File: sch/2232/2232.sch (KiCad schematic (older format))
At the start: 74 parts, among them J1 47346-0001, J2 IDC-06, J3 IDC-06, J4 IDC-10, J5 IDC-10, J6 6P6C, J7 Screw_Terminal_01x06, J8 Screw_Terminal_01x06, Q1 BC817-40, Q2 FZT1049A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

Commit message: Minor updates
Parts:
- R11, R12, R13, R8: value 100 -> 110
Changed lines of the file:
@@
 P 7600 2700
 F 0 "R8" V 7390 2700 50  0000 C CNN
-F 1 "100" V 7483 2700 50  0000 C CNN
+F 1 "110" V 7483 2700 50  0000 C CNN
 F 2 "NevaDA:R_0603" V 7530 2700 50  0001 C CNN
 F 3 "~" H 7600 2700 50  0001 C CNN
@@
 P 8000 2350
 F 0 "R13" H 8070 2397 50  0000 L CNN
-F 1 "100" H 8070 2304 50  0000 L CNN
+F 1 "110" H 8070 2304 50  0000 L CNN
 F 2 "NevaDA:R_0603" V 7930 2350 50  0001 C CNN
 F 3 "~" H 8000 2350 50  0001 C CNN
@@
 P 7150 2950
 F 0 "R11" H 7220 2997 50  0000 L CNN
-F 1 "100" H 7220 2904 50  0000 L CNN
+F 1 "110" H 7220 2904 50  0000 L CNN
 F 2 "NevaDA:R_0603" V 7080 2950 50  0001 C CNN
 F 3 "~" H 7150 2950 50  0001 C CNN
@@
 P 7150 3250
 F 0 "R12" H 7220 3297 50  0000 L CNN
-F 1 "100" H 7220 3204 50  0000 L CNN
+F 1 "110" H 7220 3204 50  0000 L CNN
 F 2 "NevaDA:R_0603" V 7080 3250 50  0001 C CNN
 F 3 "~" H 7150 3250 50  0001 C CNN

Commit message: Gerbers exported
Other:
- note added: "Sticky Pads virtual objects"
- moved on the sheet: C14, C15, C16, C17, C18, D1, D2, D3, D4, D5, D6, D7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

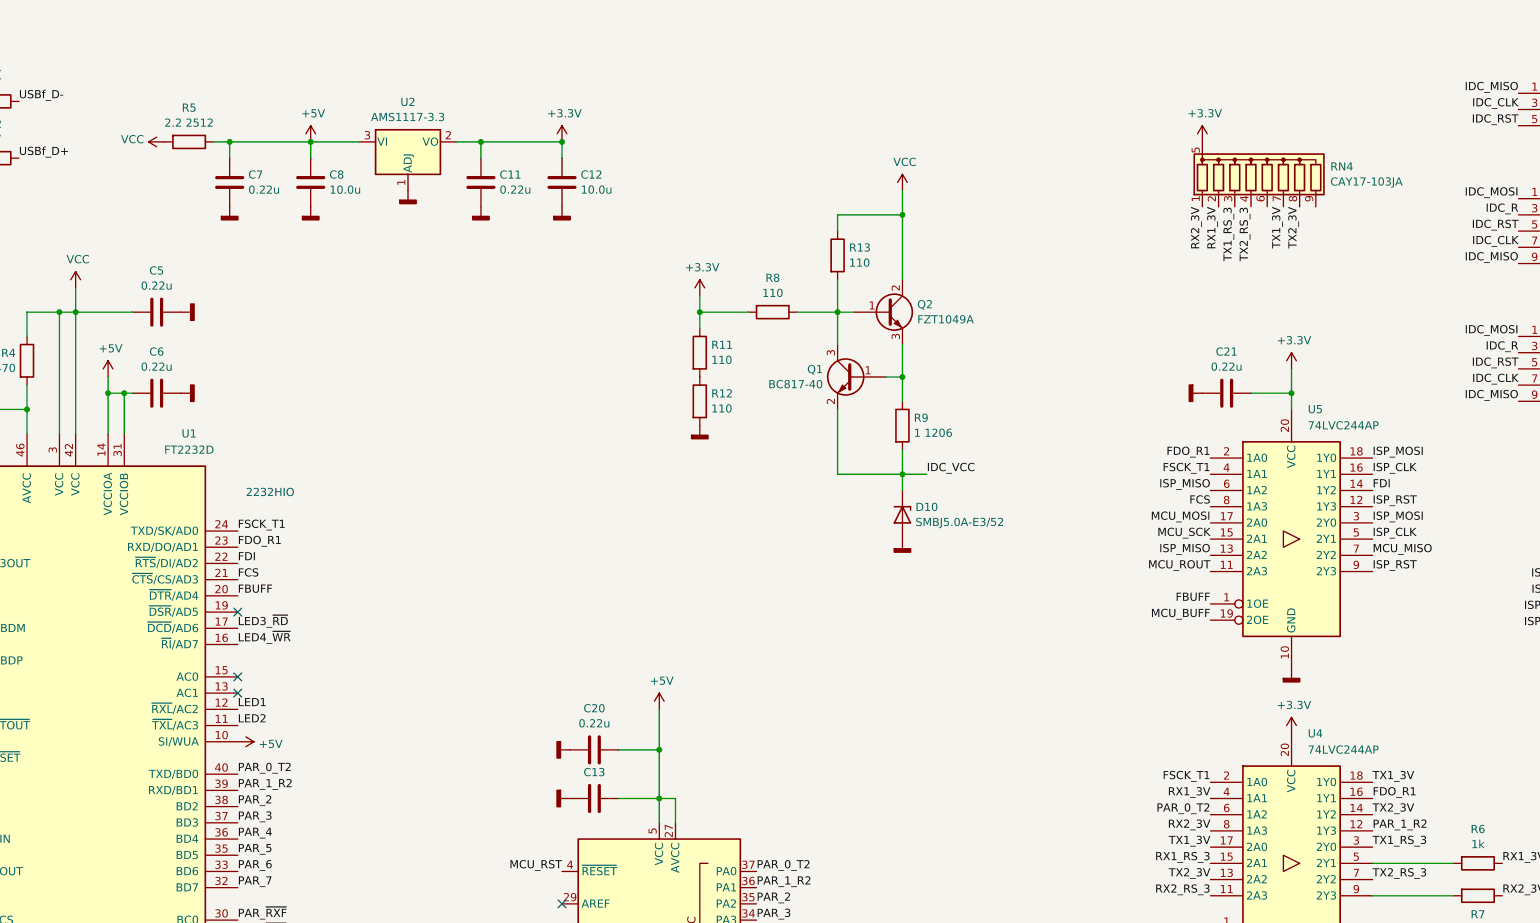
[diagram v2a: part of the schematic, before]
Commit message: Pullups to RST and MISO added
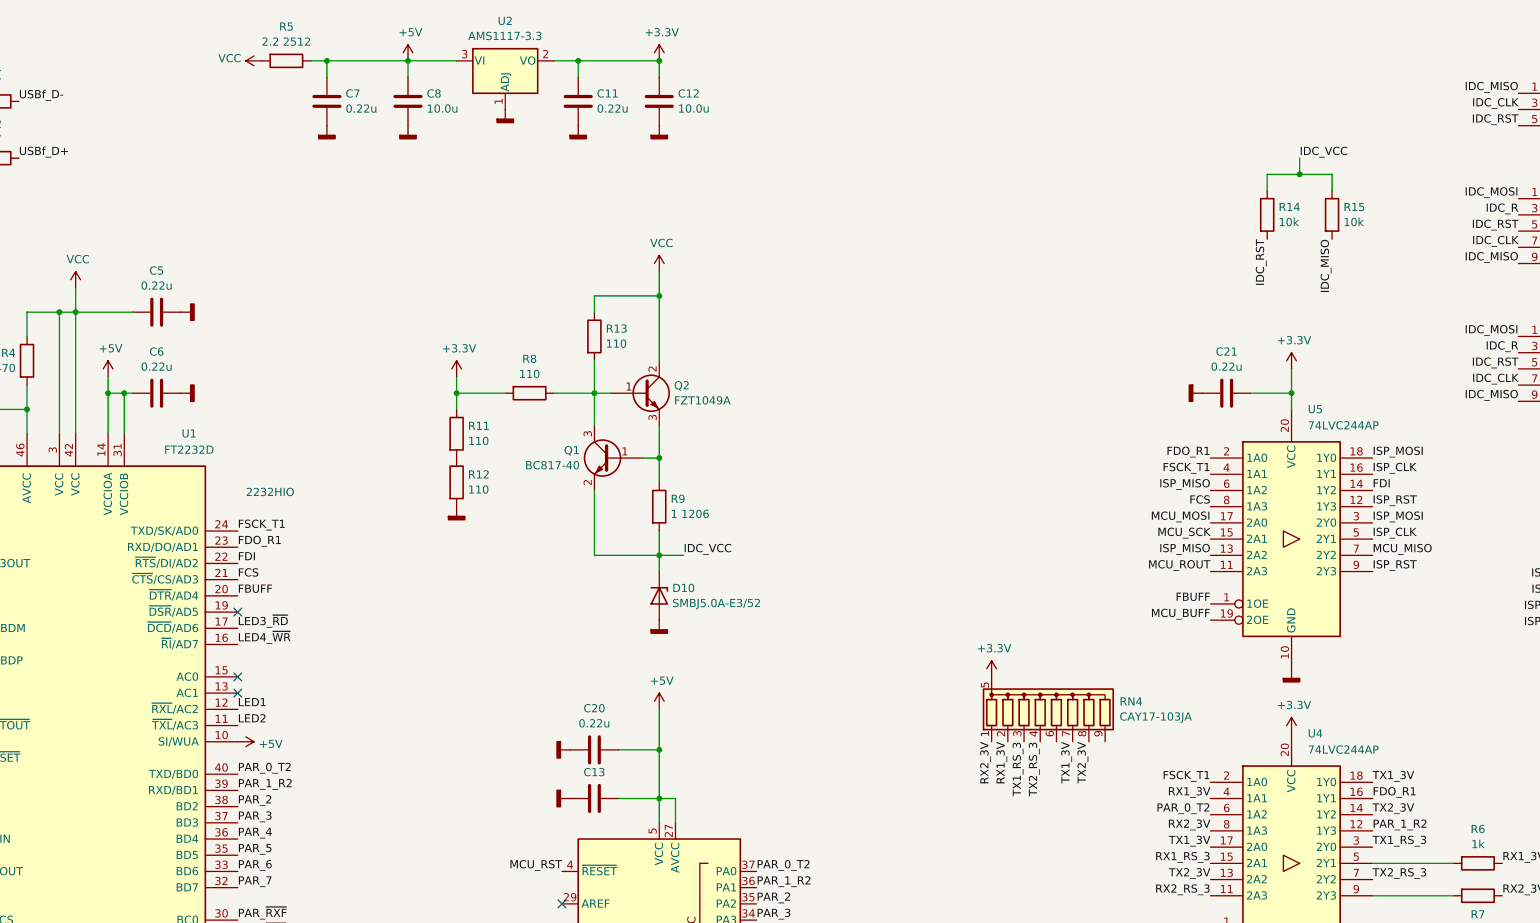
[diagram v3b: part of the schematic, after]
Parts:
- added R14, R15: 10k, NevaDA:R_0603, symbol Device:R
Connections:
- net IDC_MISO: now also R15.2
- net IDC_RST: now also R14.2
- net IDC_VCC: now also R14.1, R15.1
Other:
- moved on the sheet: C11, C12, C7, C8, D10, Q1, Q2, R11, R12, R13, R5, R8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

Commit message: Reset button added
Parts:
- added SW1: Button 6mm, NevaDA:SW_PUSH_6mm, symbol Switch:SW_SPST
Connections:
- net GNDD: now also SW1.1 (A)
- net IDC_RST: now also SW1.2 (B)
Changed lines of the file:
@@
+	1    0    0    -1
+$EndComp
+$Comp
+L Switch:SW_SPST SW1
+U 1 1 5FEB5738
+P 9850 2100
+F 0 "SW1" V 9897 2011 50  0000 R CNN
+F 1 "Button 6mm" V 9804 2011 50  0000 R CNN
+F 2 "NevaDA:SW_PUSH_6mm" H 9850 2100 50  0001 C CNN
+F 3 "~" H 9850 2100 50  0001 C CNN
+	1    9850 2100
+	0    -1   -1   0
+$EndComp
+Text Label 9850 1900 1    50   ~ 0
+IDC_RST
+$Comp
+L power:GNDD #PWR0170
+U 1 1 5FEB71AD
+P 9850 2300
+F 0 "#PWR0170" H 9850 2050 50  0001 C CNN
+F 1 "GNDD" V 9854 2190 50  0001 R CNN
+F 2 "" H 9850 2300 50  0001 C CNN
+F 3 "" H 9850 2300 50  0001 C CNN
+	1    9850 2300
 	1    0    0    -1
 $EndComp
